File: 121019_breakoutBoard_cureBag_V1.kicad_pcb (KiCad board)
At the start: 2 copper layers, 60.1 x 38.4 mm, 30 parts, among them J10 LED, J3 UART_WSG_DEBUG, J4 JTAG_SIGFOX, J6 UART_ESP_DEBUG, J7 JTAG_NRF, J8 JTAG_ESP, J9 GPIOs, SW1 SW_Push, U1 GY-BME280, U2 WSG303S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

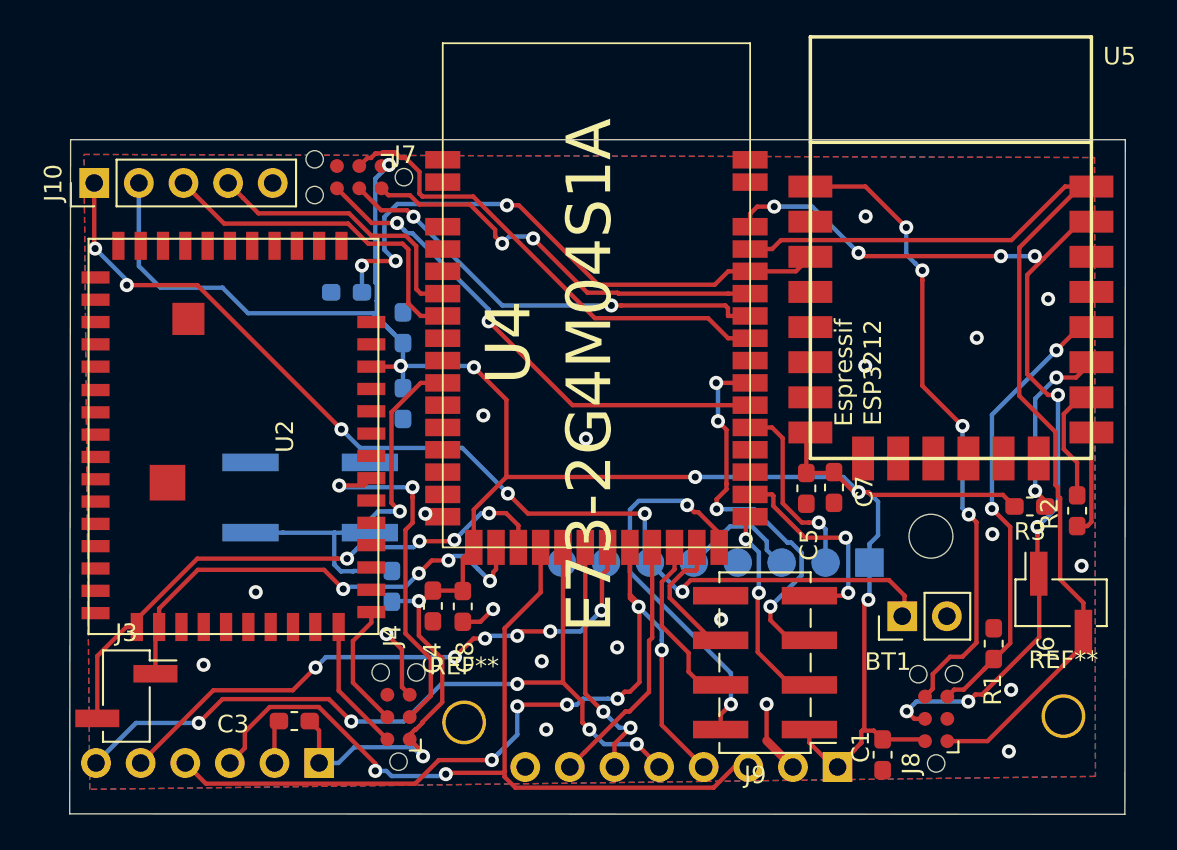
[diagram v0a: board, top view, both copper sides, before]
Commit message: fix(lipoRider): change lipo rider footprint
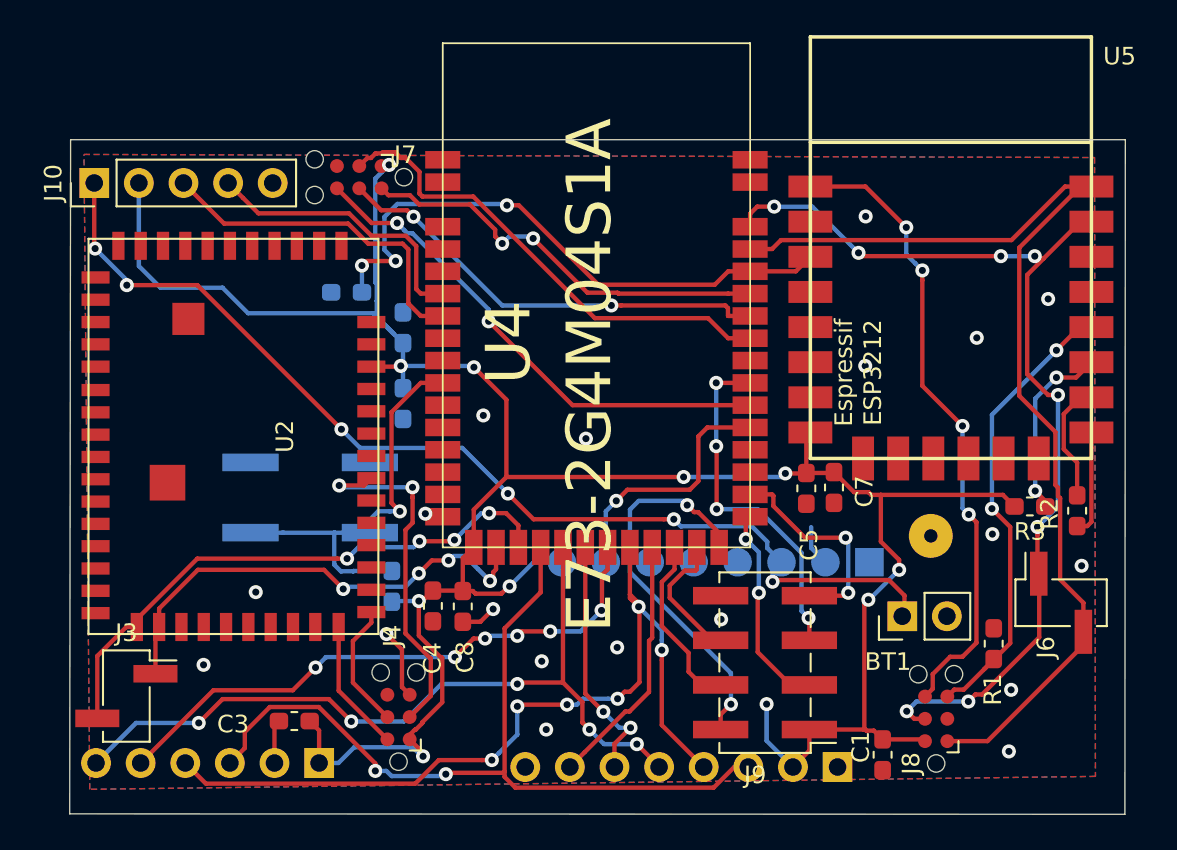
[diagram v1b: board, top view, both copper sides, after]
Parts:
- removed REF** (x2): MountingHole_2.1mm, MountingHole:MountingHole_2.1mm
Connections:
- U3 pad 1: +3V3 -> GND
- U3 pad 2: GND -> +3V3
- U6 pad 1: +3V3 -> Net-(U6-Pad1)
- U6 pad 2: /En_Bat -> GND
- U6 pad 3: GND -> /Vbat
- U6 pad 4: Net-(U6-Pad4) -> GND
- U6 pad 5: GND -> Net-(U6-Pad5)
- U6 pad 6: /Vbat -> GND
- U6 pad 7: GND -> /En_Bat
- U6 pad 8: Net-(U6-Pad8) -> +3V3
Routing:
- net GND: track 26.8 -> 18.6 mm, vias 20 -> 19
- net +3V3: track 139.6 -> 146.8 mm, vias 8 -> 11
- net /En_Bat: track 10.8 -> 14.6 mm
- net /P0.19: track 22.7 -> 20.2 mm
